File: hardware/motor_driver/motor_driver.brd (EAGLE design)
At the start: 93.7 x 72.4 mm, 88 parts

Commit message: Made the changes mike suggested
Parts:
- R19: value 10M -> 1M
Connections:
- net DGND: now also C11.1
- net GND: no longer C11.1
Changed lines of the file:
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@@
 <element name="R17" library="adafruit" package="R0603" value="270K" x="36.83" y="33.02" rot="MR270"/>
 <element name="R18" library="adafruit" package="R0603" value="10K" x="39.37" y="38.1" rot="MR90"/>
-<element name="R19" library="adafruit" package="R0603" value="10M" x="50.8" y="29.21"/>
+<element name="R19" library="adafruit" package="R0603" value="1M" x="50.8" y="29.21"/>
 <element name="R2" library="adafruit" package="R0603" value="4.7K" x="68.58" y="3.81" rot="MR180"/>
 <element name="R20" library="adafruit" package="R0603" value="15K" x="33.02" y="24.13" rot="R90"/>
@@
 <contactref element="U$9" pad="P$1@2"/>
 <contactref element="R13" pad="2"/>
-<contactref element="C11" pad="1"/>
 <contactref element="C12" pad="2"/>
 <contactref element="C13" pad="2"/>
@@
 <wire x1="43.18" y1="39.24" x2="45.72" y2="39.24" width="0" layer="19" extent="16-16"/>
 <wire x1="50.8" y1="41.78" x2="45.72" y2="39.24" width="0" layer="19" extent="16-16"/>
-<wire x1="43.05" y1="10.16" x2="46.98" y2="17.3" width="0" layer="19" extent="1-1"/>
 <wire x1="25.4" y1="67.945" x2="43.18" y2="39.24" width="0" layer="19" extent="1-16"/>
-<wire x1="22.86" y1="70.485" x2="25.4" y2="69.215" width="0" layer="19" extent="1-1"/>
+<wire x1="22.86" y1="69.215" x2="25.4" y2="69.215" width="0" layer="19" extent="1-1"/>
 </signal>
 <signal name="SO2">
@@
 <contactref element="C27" pad="2"/>
 <contactref element="TEMP" pad="1"/>
+<contactref element="C11" pad="1"/>
 <wire x1="42.1386" y1="51.3588" x2="50.8" y2="51.48" width="0" layer="19" extent="16-16"/>
 <wire x1="42.55" y1="54.61" x2="42.1386" y2="51.3588" width="0" layer="19" extent="16-16"/>
 <wire x1="37.68" y1="52.07" x2="42.1386" y2="51.3588" width="0" layer="19" extent="16-16"/>
 <wire x1="37.46" y1="57.15" x2="37.68" y2="52.07" width="0" layer="19" extent="16-16"/>
+<wire x1="33.9" y1="66.04" x2="37.46" y2="57.15" width="0" layer="19" extent="16-16"/>
+<wire x1="25.4" y1="67.945" x2="33.9" y2="66.04" width="0" layer="19" extent="1-16"/>
+<wire x1="16.51" y1="66.04" x2="25.4" y2="67.945" width="0" layer="19" extent="1-1"/>
+<wire x1="16.51" y1="60.96" x2="16.51" y2="66.04" width="0" layer="19" extent="1-1"/>
+<wire x1="16.51" y1="55.88" x2="16.51" y2="60.96" width="0" layer="19" extent="1-1"/>
 <wire x1="38.1" y1="42.33" x2="37.68" y2="52.07" width="0" layer="19" extent="1-16"/>
 <wire x1="39.37" y1="37.25" x2="38.1" y2="42.33" width="0" layer="19" extent="1-16"/>
@@
 <wire x1="30.48" y1="24.98" x2="30.9" y2="26.67" width="0" layer="19" extent="1-1"/>
 <wire x1="32.17" y1="21.59" x2="30.48" y2="24.98" width="0" layer="19" extent="1-1"/>
-<wire x1="33.9" y1="66.04" x2="37.46" y2="57.15" width="0" layer="19" extent="16-16"/>
-<wire x1="16.51" y1="66.04" x2="33.9" y2="66.04" width="0" layer="19" extent="16-16"/>
-<wire x1="16.51" y1="60.96" x2="16.51" y2="66.04" width="0" layer="19" extent="1-1"/>
-<wire x1="16.51" y1="55.88" x2="16.51" y2="60.96" width="0" layer="19" extent="1-1"/>
+<wire x1="43.05" y1="10.16" x2="32.17" y2="21.59" width="0" layer="19" extent="1-1"/>
+<wire x1="50.8" y1="3.81" x2="43.05" y2="10.16" width="0" layer="19" extent="1-1"/>
+<wire x1="56.2" y1="2.54" x2="50.8" y2="3.81" width="0" layer="19" extent="1-1"/>
+<wire x1="56.3" y1="5.08" x2="56.2" y2="2.54" width="0" layer="19" extent="1-1"/>
 <wire x1="12.7" y1="38.1" x2="16.51" y2="55.88" width="0" layer="19" extent="1-1"/>
 <wire x1="12.7" y1="7.62" x2="32.17" y2="21.59" width="0" layer="19" extent="1-1"/>
-<wire x1="56.3" y1="5.08" x2="49.95" y2="29.21" width="0" layer="19" extent="1-1"/>
-<wire x1="56.2" y1="2.54" x2="56.3" y2="5.08" width="0" layer="19" extent="1-1"/>
-<wire x1="50.8" y1="3.81" x2="56.2" y2="2.54" width="0" layer="19" extent="1-1"/>
-<wire x1="25.4" y1="67.945" x2="16.51" y2="66.04" width="0" layer="19" extent="1-1"/>
 </signal>
 <signal name="+5V">

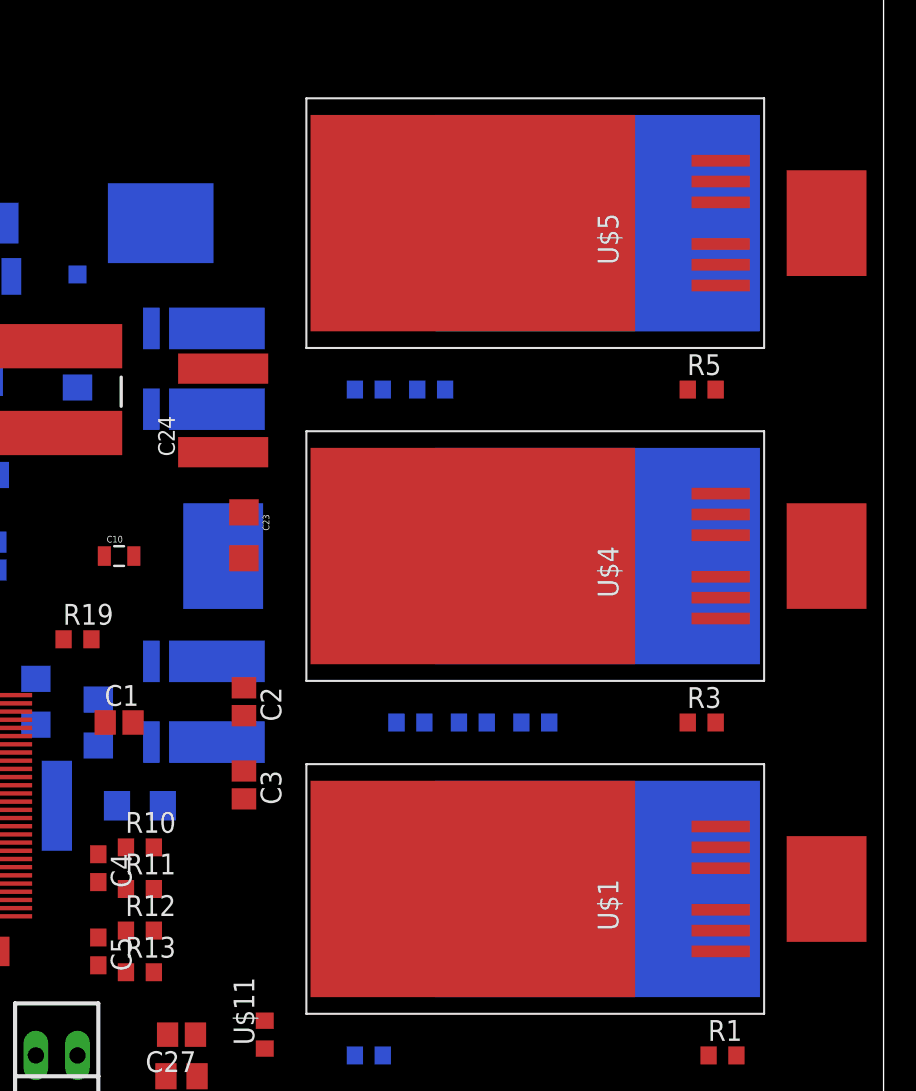
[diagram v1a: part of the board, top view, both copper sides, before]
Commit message: First commit on Mike's branch. Starting board layout. Rumman is doing the same.
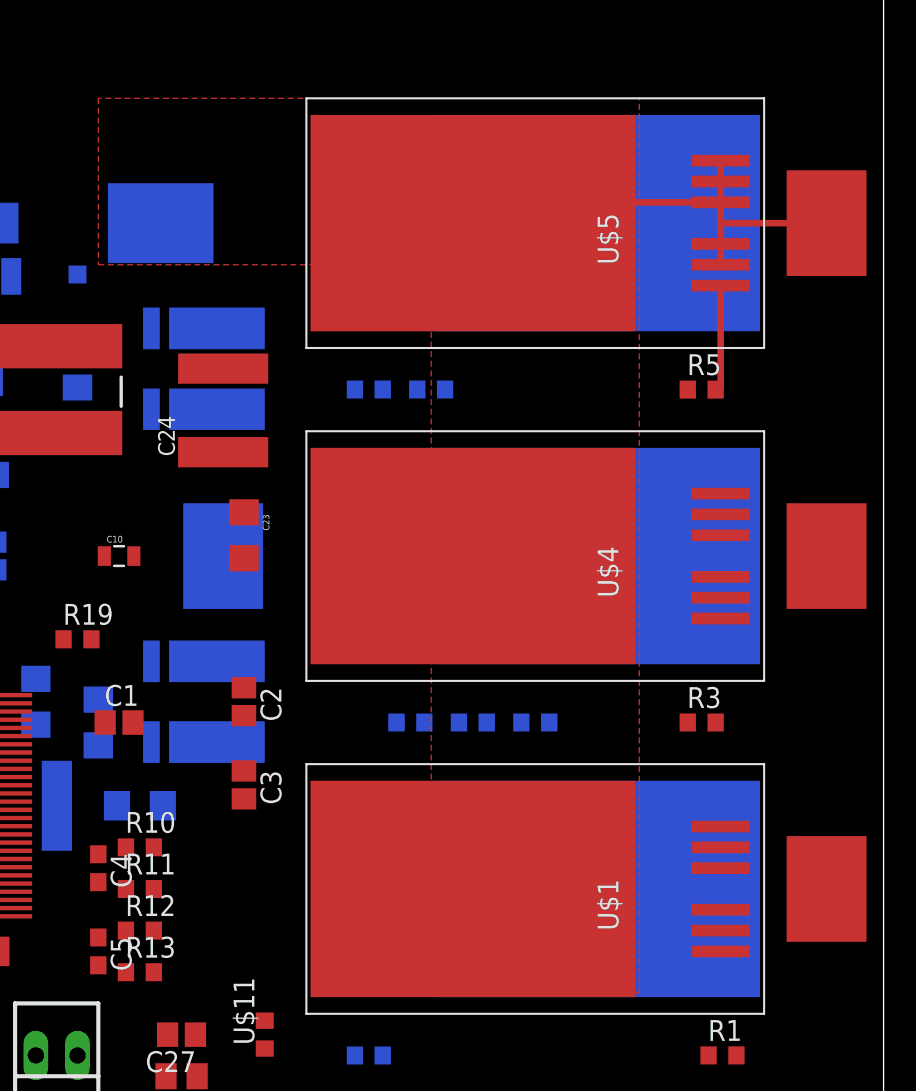
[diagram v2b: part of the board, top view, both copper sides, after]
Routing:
- net H3_VS: track 0.00 -> 22.1 mm
- net N$5: track 0.00 -> 6.48 mm
- added copper zone on layer 1, net N$9
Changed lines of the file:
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@@
 <?xml version="1.0" encoding="utf-8"?>
 <!DOCTYPE eagle SYSTEM "eagle.dtd">
-<eagle version="7.3.0">
+<eagle version="7.2.0">
 <drawing>
 <settings>
@@
 <layers>
 <layer number="1" name="Top" color="4" fill="1" visible="yes" active="yes"/>
-<layer number="16" name="Bottom" color="1" fill="1" visible="yes" active="yes"/>
+<layer number="16" name="Bottom" color="1" fill="1" visible="no" active="yes"/>
 <layer number="17" name="Pads" color="2" fill="1" visible="yes" active="yes"/>
 <layer number="18" name="Vias" color="2" fill="1" visible="yes" active="yes"/>
@@
 <contactref element="R5" pad="2"/>
 <contactref element="U$5" pad="G1"/>
-<wire x1="89.75" y1="44.45" x2="90.0557" y2="50.8" width="0" layer="19" extent="1-1"/>
+<wire x1="90.0557" y1="50.8" x2="90.0557" y2="44.7557" width="0.4064" layer="1"/>
+<wire x1="90.0557" y1="44.7557" x2="89.75" y2="44.45" width="0.4064" layer="1"/>
 </signal>
 <signal name="N$6">
@@
 <contactref element="R30" pad="1"/>
 <contactref element="U$12" pad="P$1"/>
-<wire x1="90.0557" y1="55.88" x2="96.52" y2="54.61" width="0" layer="19" extent="1-1"/>
-<wire x1="90.0557" y1="57.15" x2="90.0557" y2="55.88" width="0" layer="19" extent="1-1"/>
-<wire x1="90.0557" y1="58.42" x2="90.0557" y2="57.15" width="0" layer="19" extent="1-1"/>
-<wire x1="90.0557" y1="53.34" x2="90.0557" y2="55.88" width="0" layer="19" extent="1-1"/>
-<wire x1="90.0557" y1="52.07" x2="90.0557" y2="53.34" width="0" layer="19" extent="1-1"/>
-<wire x1="82.55" y1="54.61" x2="90.0557" y2="55.88" width="0" layer="19" extent="1-16"/>
 <wire x1="60.96" y1="19.47" x2="82.55" y2="54.61" width="0" layer="19" extent="1-16"/>
 <wire x1="46.98" y1="15.8" x2="60.96" y2="19.47" width="0" layer="19" extent="1-1"/>
 <wire x1="25.4" y1="51.8" x2="46.98" y2="15.8" width="0" layer="19" extent="1-16"/>
+<wire x1="96.52" y1="54.61" x2="90.0557" y2="54.61" width="0.4064" layer="1"/>
+<wire x1="90.0557" y1="54.61" x2="90.0557" y2="55.88" width="0.4064" layer="1"/>
+<wire x1="90.0557" y1="55.88" x2="90.0557" y2="57.15" width="0.4064" layer="1"/>
+<wire x1="90.0557" y1="57.15" x2="90.0557" y2="58.42" width="0.4064" layer="1"/>
+<wire x1="90.0557" y1="55.88" x2="90.0557" y2="53.34" width="0.4064" layer="1"/>
+<wire x1="90.0557" y1="53.34" x2="90.0557" y2="52.07" width="0.4064" layer="1"/>
+<wire x1="90.0557" y1="55.88" x2="83.82" y2="55.88" width="0.4064" layer="1"/>
+<wire x1="83.82" y1="55.88" x2="82.55" y2="54.61" width="0.4064" layer="1"/>
+<wire x1="82.55" y1="54.61" x2="82.55" y2="54.61" width="0" layer="19" extent="1-16"/>
 </signal>
 <signal name="H1_LOW">
@@
 <wire x1="48.26" y1="3.81" x2="58" y2="5.08" width="0" layer="19" extent="1-1"/>
 </signal>
+<signal name="N$9">
+<polygon width="0.4064" layer="1">
+<vertex x="72.39" y="7.62"/>
+<vertex x="85.09" y="7.62"/>
+<vertex x="85.09" y="62.23"/>
+<vertex x="52.07" y="62.23"/>
+<vertex x="52.07" y="52.07"/>
+<vertex x="72.39" y="52.07"/>
+</polygon>
+</signal>
 </signals>

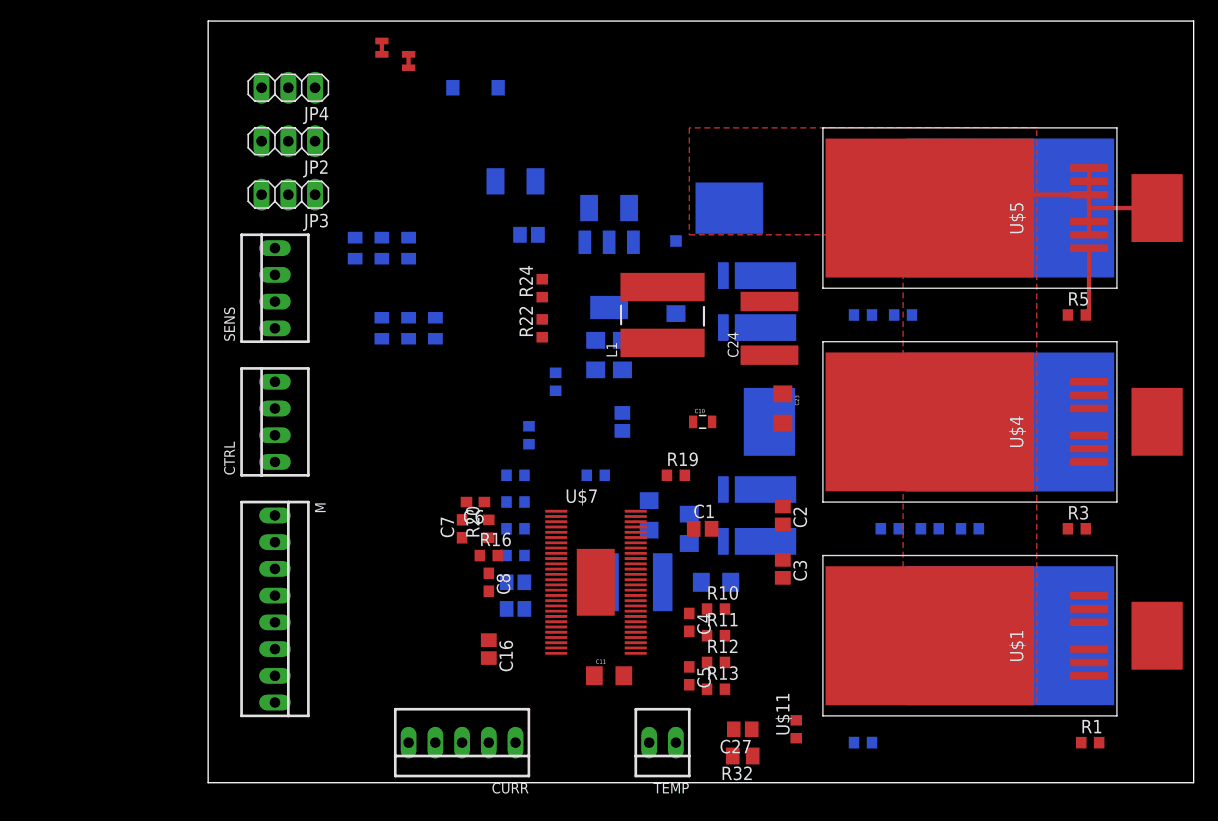
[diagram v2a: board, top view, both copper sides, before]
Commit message: Board route (manual) trial number 1
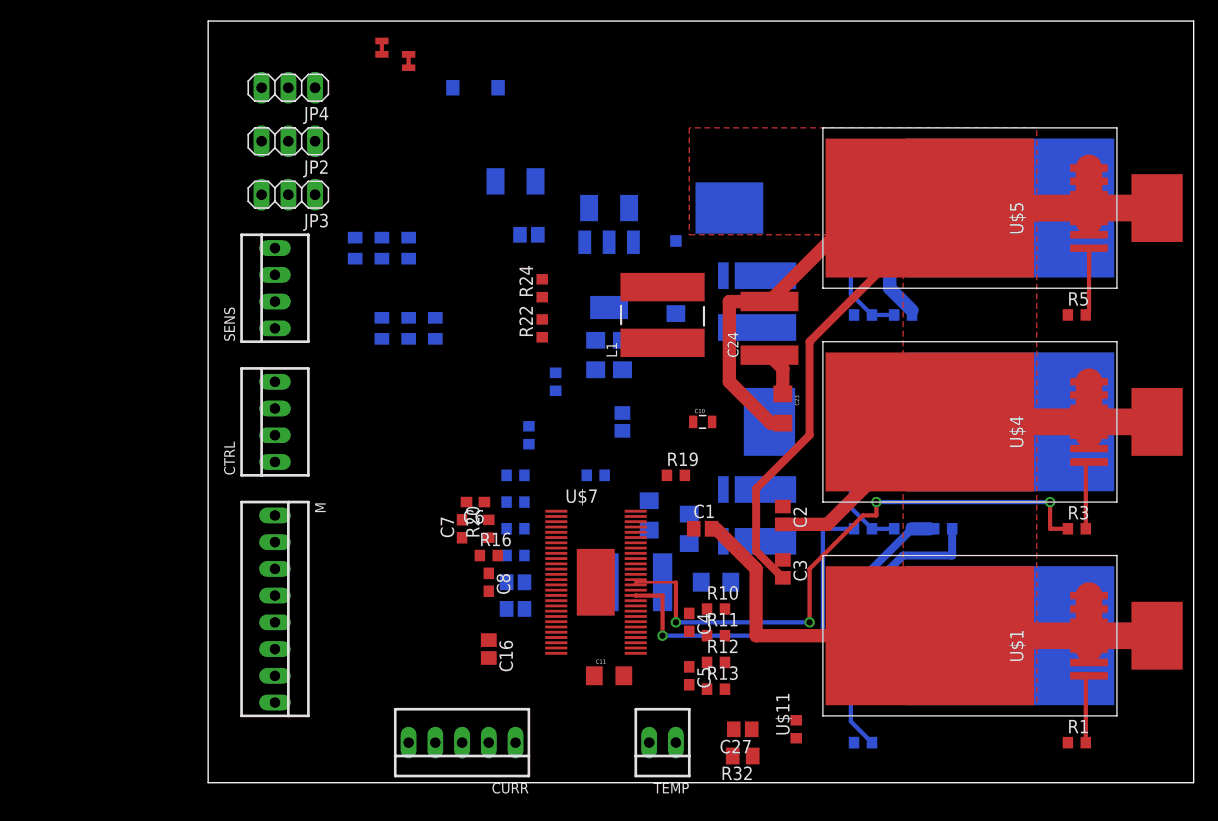
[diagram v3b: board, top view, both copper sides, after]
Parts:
- moved R4 2.54 mm to (68.6, 24.1)
- moved R8 2.54 mm to (72.4, 24.1)
- moved R9 2.54 mm to (76.2, 24.1)
- moved R1 1.27 mm to (88.9, 3.81)
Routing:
- net GH_B: track 0.00 -> 56.1 mm, vias 0 -> 4
- net H1_VS: track 0.00 -> 54.9 mm
- net H3_VS: track 22.1 -> 67.7 mm
- net H2_VS: track 0.00 -> 44.7 mm
- net VCC: track 0.00 -> 37.1 mm
- net GL_B: track 0.00 -> 34.7 mm, vias 0 -> 1
- net N$2: track 0.00 -> 30.0 mm
- net H3_LOW: track 0.00 -> 16.9 mm
- net H1_LOW: track 0.00 -> 15.5 mm
- net GND: track 0.00 -> 9.28 mm
- net N$3: track 0.00 -> 8.87 mm
- net N$6: track 0.00 -> 8.87 mm
- net N$4: track 0.00 -> 6.66 mm
- net N$1: track 0.00 -> 6.66 mm

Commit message: small change
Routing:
- net GH_B: track 56.1 -> 55.4 mm
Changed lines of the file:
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@@
 <via x="69.85" y="26.67" extent="1-16" drill="0.6" shape="square"/>
 <wire x1="69.85" y1="26.67" x2="69.85" y2="25.4" width="0.4064" layer="1"/>
-<wire x1="60.96" y1="16.51" x2="46.98" y2="18.8" width="0" layer="19" extent="1-16"/>
 <wire x1="69.85" y1="25.4" x2="68.58" y2="25.4" width="0.4064" layer="1"/>
 <wire x1="68.58" y1="25.4" x2="63.5" y2="20.32" width="0.4064" layer="1"/>
@@
 <wire x1="63.5" y1="15.24" x2="50.8" y2="15.24" width="0.4064" layer="16"/>
 <via x="50.8" y="15.24" extent="1-16" drill="0.6" shape="square"/>
-<wire x1="50.8" y1="15.24" x2="50.8" y2="19.05" width="0.4064" layer="1"/>
-<wire x1="50.8" y1="19.05" x2="46.98" y2="19.05" width="0.254" layer="1"/>
-<wire x1="46.98" y1="19.05" x2="46.98" y2="18.8" width="0.254" layer="1"/>
+<wire x1="50.8" y1="15.24" x2="50.8" y2="18.415" width="0.3048" layer="1"/>
+<wire x1="50.8" y1="18.415" x2="50.415" y2="18.8" width="0.3048" layer="1"/>
+<wire x1="50.415" y1="18.8" x2="46.98" y2="18.8" width="0.3048" layer="1"/>
 </signal>
 <signal name="GH_C">

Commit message: Shit from Sunday work session
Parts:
- moved U$2 7.62 mm to (88.9, 14.0)
- moved U$3 7.62 mm to (88.9, 34.3)
- moved U$6 7.62 mm to (88.9, 54.6)
- moved C16 6.84 mm to (39.4, 10.2), turned to 0 degrees
- moved C24 5.68 mm to (62.2, 48.3)
- moved U$15 5.68 mm to (58.4, 59.7)
- moved U$8 5.68 mm to (61.0, 20.3)
- moved U$9 5.68 mm to (61.0, 50.8)
- moved R3 2.84 mm to (91.4, 25.4)
- moved C8 2.62 mm to (33.7, 21.6), turned to 180 degrees
- moved R16 2.54 mm to (30.5, 21.6)
- moved R15 2.54 mm to (33.0, 21.6)
- moved R1 2.54 mm to (91.4, 3.81)
- moved R5 2.54 mm to (91.4, 44.5)
- moved U$1 2.54 mm to (78.7, 14.0)
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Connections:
- net DC_CAL: now also CURR.4; no longer CURR.2
- net DGND: now also M.1; no longer M.8
- net EN_GATE: now also M.2; no longer M.1
- net H1: now also M.3; no longer M.2
- net H2: now also M.5; no longer M.4
- net H3: now also M.7; no longer M.6
- net L1: now also M.4; no longer M.3
- net L2: now also M.6; no longer M.5
- net L3: now also M.8; no longer M.7
- net REF: now also CURR.3; no longer CURR.1
- net SO1: now also CURR.2; no longer CURR.3
- net SO2: now also CURR.1; no longer CURR.4
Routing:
- net DGND: track 0.00 -> 135.6 mm, vias 0 -> 1
- net AGND: track 0.00 -> 117.1 mm, vias 0 -> 3
- net H3_VS: track 67.7 -> 0.00 mm
- net H1_VS: track 54.9 -> 0.00 mm
- net H2_VS: track 44.7 -> 0.00 mm
- net FAULT: track 0.00 -> 39.7 mm, vias 0 -> 2
- net +5V: track 0.00 -> 37.0 mm, vias 0 -> 2
- net PWRGD: track 0.00 -> 30.0 mm, vias 0 -> 2
- net L3: track 0.00 -> 29.9 mm
- net H3: track 0.00 -> 29.3 mm
- net EN_GATE: track 0.00 -> 28.6 mm
- net L2: track 0.00 -> 28.2 mm
- net H1: track 0.00 -> 27.8 mm
- net H2: track 0.00 -> 27.4 mm
- net L1: track 0.00 -> 27.0 mm
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- added copper zone on layer 1, net DGND
- added copper zone on layer 1, net H1_VS
- added copper zone on layer 1, net H2_VS
- added copper zone on layer 1, net H3_VS
- added copper zone on layer 1, net N$122
- added copper zone on layer 1, net N$125
- added copper zone on layer 1, net N$43
- added copper zone on layer 16, net N$97
- added copper zone on layer 16, net N$98
- added copper zone on layer 16, net N$99

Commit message: more board layout done, still need to fix resistor package
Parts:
- moved C22 3.81 mm to (43.2, 19.1)
- moved C3 1.59 mm to (61.0, 18.7), turned to 90 degrees
- moved R13 1.27 mm to (54.6, 7.62)
- moved C4 1.27 mm to (52.1, 14.0)
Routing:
- net H3_VS: track 0.00 -> 74.6 mm, vias 0 -> 2
- net VCC: track 34.4 -> 58.5 mm, vias 1 -> 2
- net GL_C: track 0.00 -> 21.7 mm, vias 0 -> 2
- net N$26: track 0.00 -> 15.4 mm, vias 0 -> 2
- net H3_LOW: track 0.00 -> 11.3 mm, vias 0 -> 2
- net N$11: track 0.00 -> 9.42 mm
- net N$24: track 0.00 -> 8.15 mm
- net N$22: track 0.00 -> 7.92 mm
- net N$6: track 1.69 -> 9.49 mm
- net GND: track 26.3 -> 34.1 mm
- net N$23: track 0.00 -> 7.41 mm
- net GL_B: track 35.0 -> 27.7 mm, vias 1 -> 2
- net GH_B: track 50.2 -> 46.3 mm, vias 1 -> 2
- net N$3: track 5.53 -> 1.69 mm
- net N$2: track 33.4 -> 30.5 mm
- added copper zone on layer 16, net H3_LOW
- removed copper zone on layer 16, net N$97
